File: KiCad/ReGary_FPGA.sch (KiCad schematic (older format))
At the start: 28 parts, among them J1 Conn_01x02, U1 GW1N-UV1P5LQ100, U2 LM1117-3.3, U3 TPS73643DBV

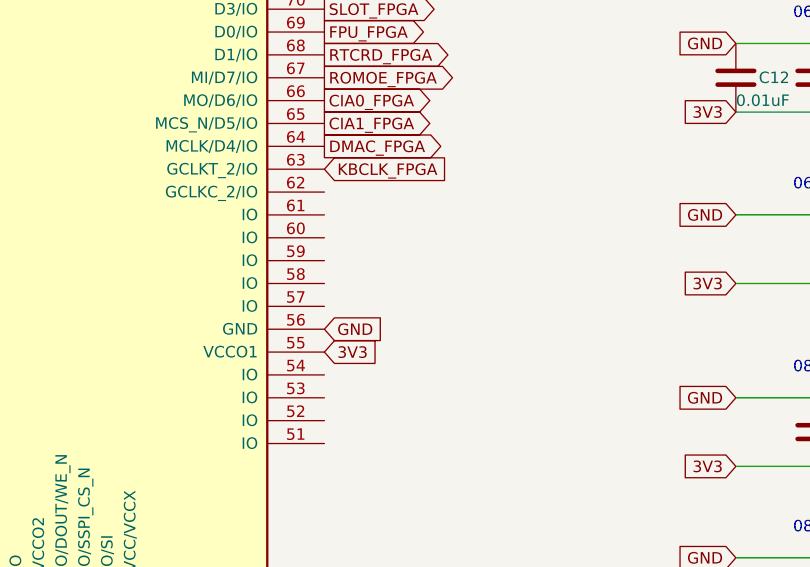
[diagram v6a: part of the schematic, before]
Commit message: More pin assignments and routing
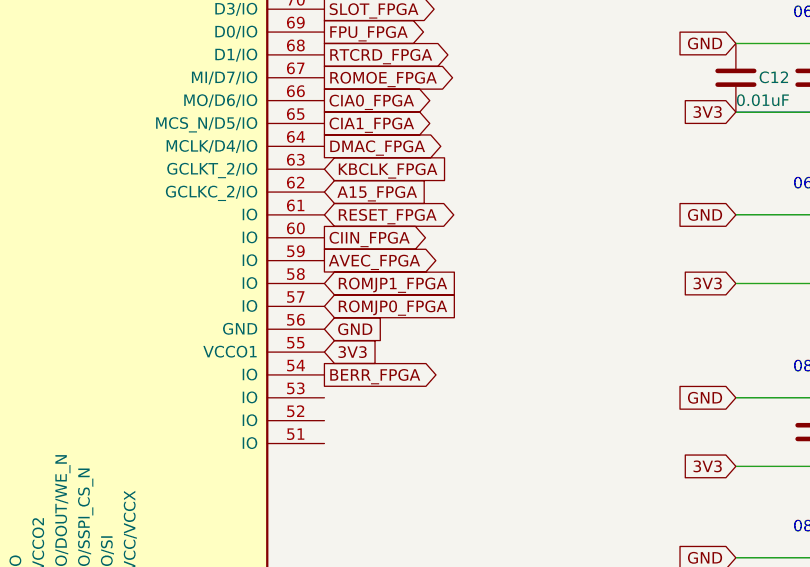
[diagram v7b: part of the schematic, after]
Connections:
- net labels added: A15_FPGA, AVEC_FPGA, BERR_FPGA, CIIN_FPGA, RESET_FPGA, ROMJP0_FPGA, ROMJP1_FPGA
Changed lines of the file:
@@
 Text GLabel 2600 2100 1    50   Output ~ 0
 BLS_FPGA
+Text GLabel 5450 4450 2    50   Output ~ 0
+CIIN_FPGA
+Text GLabel 5450 5050 2    50   Output ~ 0
+BERR_FPGA
+Text GLabel 5450 4550 2    50   Output ~ 0
+AVEC_FPGA
+Text GLabel 5450 4650 2    50   Input ~ 0
+ROMJP1_FPGA
+Text GLabel 5450 4750 2    50   Input ~ 0
+ROMJP0_FPGA
+Text GLabel 5450 4350 2    50   BiDi ~ 0
+RESET_FPGA
+Text GLabel 5450 4250 2    50   Input ~ 0
+A15_FPGA
 $EndSCHEMATC

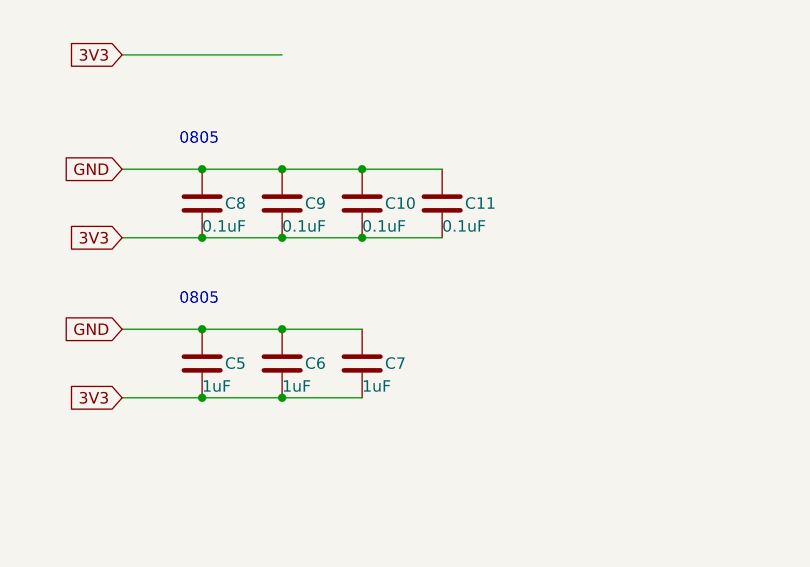
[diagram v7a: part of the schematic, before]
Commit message: Placement of caps and more routing of 3V3-power
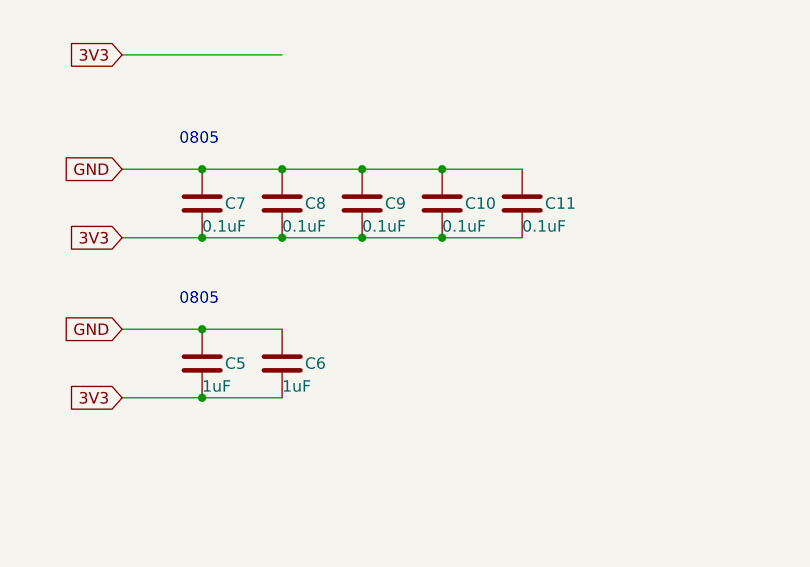
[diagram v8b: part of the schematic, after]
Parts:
- C11: renamed from C7; value 1uF -> 0.1uF
- renumbered C11 to C10, C8 to C7, C10 to C8
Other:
- moved on the sheet: C11, C8, C9
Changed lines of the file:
@@
 L Device:C C?
 U 1 1 60CC8F0E
-P 7950 5300
+P 8300 5300
 AR Path="/60CC8F0E" Ref="C?"  Part="1"
 AR Path="/608A10F5/60CC8F0E" Ref="C9"  Part="1"
-F 0 "C9" H 8050 5300 50  0000 L CNN
-F 1 "0.1uF" H 7950 5200 50  0000 L CNN
-F 2 "Capacitor_SMD:C_0805_2012Metric_Pad1.18x1.45mm_HandSolder" H 7988 5150 50  0001 C CNN
-F 3 "~" H 7950 5300 50  0001 C CNN
-	1    7950 5300
+F 0 "C9" H 8400 5300 50  0000 L CNN
+F 1 "0.1uF" H 8300 5200 50  0000 L CNN
+F 2 "Capacitor_SMD:C_0805_2012Metric_Pad1.18x1.45mm_HandSolder" H 8338 5150 50  0001 C CNN
+F 3 "~" H 8300 5300 50  0001 C CNN
+	1    8300 5300
 	1    0    0    -1
 $EndComp
@@
 P 8650 5300
 AR Path="/607ACE36" Ref="C?"  Part="1"
-AR Path="/608A10F5/607ACE36" Ref="C11"  Part="1"
-F 0 "C11" H 8750 5300 50  0000 L CNN
+AR Path="/608A10F5/607ACE36" Ref="C10"  Part="1"
+F 0 "C10" H 8750 5300 50  0000 L CNN
 F 1 "0.1uF" H 8650 5200 50  0000 L CNN
 F 2 "Capacitor_SMD:C_0805_2012Metric_Pad1.18x1.45mm_HandSolder" H 8688 5150 50  0001 C CNN
@@
 L Device:C C?
 U 1 1 608291F3
-P 8300 5300
+P 7950 5300
 AR Path="/608291F3" Ref="C?"  Part="1"
-AR Path="/608A10F5/608291F3" Ref="C10"  Part="1"
-F 0 "C10" H 8400 5300 50  0000 L CNN
-F 1 "0.1uF" H 8300 5200 50  0000 L CNN
-F 2 "Capacitor_SMD:C_0805_2012Metric_Pad1.18x1.45mm_HandSolder" H 8338 5150 50  0001 C CNN
-F 3 "~" H 8300 5300 50  0001 C CNN
-	1    8300 5300
+AR Path="/608A10F5/608291F3" Ref="C8"  Part="1"
+F 0 "C8" H 8050 5300 50  0000 L CNN
+F 1 "0.1uF" H 7950 5200 50  0000 L CNN
+F 2 "Capacitor_SMD:C_0805_2012Metric_Pad1.18x1.45mm_HandSolder" H 7988 5150 50  0001 C CNN
+F 3 "~" H 7950 5300 50  0001 C CNN
+	1    7950 5300
 	1    0    0    -1
 $EndComp
@@
 Connection ~ 7950 5150
 Wire Wire Line
-	7950 5450 8300 5450
-Connection ~ 7950 5450
+	8300 5450 8650 5450
+Connection ~ 8300 5450
 $Comp
 L Device:C C?
@@
 L Device:C C?
 U 1 1 6084459F
-P 8300 6000
+P 9000 5300
 AR Path="/6084459F" Ref="C?"  Part="1"
-AR Path="/608A10F5/6084459F" Ref="C7"  Part="1"
-F 0 "C7" H 8400 6000 50  0000 L CNN
-F 1 "1uF" H 8300 5900 50  0000 L CNN
-F 2 "Capacitor_SMD:C_0805_2012Metric_Pad1.18x1.45mm_HandSolder" H 8338 5850 50  0001 C CNN
-F 3 "~" H 8300 6000 50  0001 C CNN
-	1    8300 6000
+AR Path="/608A10F5/6084459F" Ref="C11"  Part="1"
+F 0 "C11" H 9100 5300 50  0000 L CNN
+F 1 "0.1uF" H 9000 5200 50  0000 L CNN
+F 2 "Capacitor_SMD:C_0805_2012Metric_Pad1.18x1.45mm_HandSolder" H 9038 5150 50  0001 C CNN
+F 3 "~" H 9000 5300 50  0001 C CNN
+	1    9000 5300
 	1    0    0    -1
 $EndComp
@@
 Connection ~ 7600 5850
 Wire Wire Line
-	7950 5850 8300 5850
-Connection ~ 7950 5850
-Wire Wire Line
 	7600 6150 7950 6150
 Connection ~ 7600 6150
-Connection ~ 7950 6150
-Wire Wire Line
-	7950 6150 8300 6150
 $Comp
 L ReGary:GW1N-UV1P5LQ100 U1
@@
 P 7600 5300
 AR Path="/67F0E861" Ref="C?"  Part="1"
-AR Path="/608A10F5/67F0E861" Ref="C8"  Part="1"
-F 0 "C8" H 7700 5300 50  0000 L CNN
+AR Path="/608A10F5/67F0E861" Ref="C7"  Part="1"
+F 0 "C7" H 7700 5300 50  0000 L CNN
 F 1 "0.1uF" H 7600 5200 50  0000 L CNN
 F 2 "Capacitor_SMD:C_0805_2012Metric_Pad1.18x1.45mm_HandSolder" H 7638 5150 50  0001 C CNN
@@
 $EndComp
 Wire Wire Line
-	7250 5150 7600 5150
-Wire Wire Line
 	7250 5450 7600 5450
-Connection ~ 7600 5150
-Wire Wire Line
-	7600 5150 7950 5150
-Connection ~ 7600 5450
-Wire Wire Line
-	7600 5450 7950 5450
+Wire Wire Line
+	7950 5450 8300 5450
 $Comp
 L Device:R_Small R1
@@
 Connection ~ 8300 5150
 Wire Wire Line
-	8300 5450 8650 5450
-Connection ~ 8300 5450
+	8650 5450 9000 5450
+Connection ~ 8650 5450
 Text GLabel 4700 1750 1    50   Input ~ 0
 JTAGSEL_N
@@
 Text GLabel 5450 4250 2    50   Input ~ 0
 A15_FPGA
+Wire Wire Line
+	7250 5150 7600 5150
+Connection ~ 7600 5150
+Wire Wire Line
+	7600 5150 7950 5150
+Wire Wire Line
+	7600 5450 7950 5450
+Connection ~ 7600 5450
+Connection ~ 7950 5450
+Wire Wire Line
+	8650 5150 9000 5150
+Connection ~ 8650 5150
 $EndSCHEMATC
